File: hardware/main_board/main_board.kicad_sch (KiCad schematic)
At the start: 79 parts, among them J1 USB_C_Receptacle_USB2.0_16P, J2 UART_DEBUG, J3 BAT1, J4 Conn_02x05_Odd_Even, J5 Conn_02x05_Odd_Even, Q1 MMBT3904, Q2 MMBT3904, SW1 SW_MEC_5G, U1 MPU-6050, U10 AMS1117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

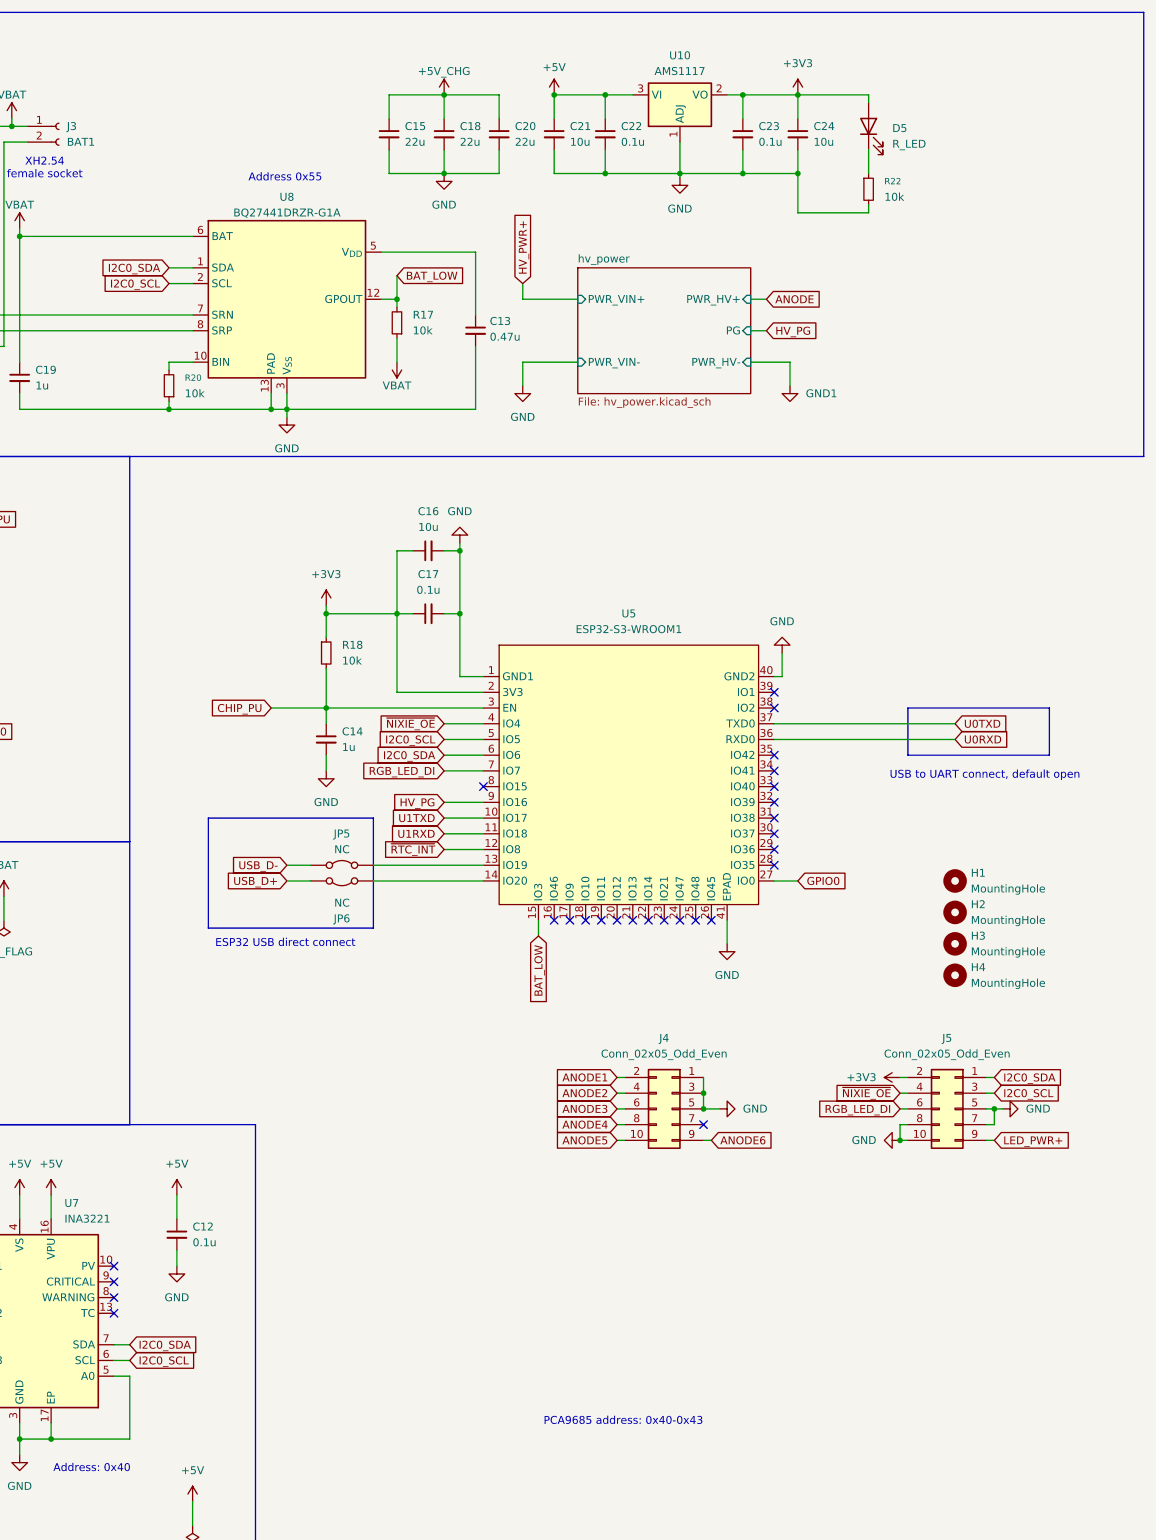
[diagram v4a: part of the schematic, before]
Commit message: WIP(haedware): add TPS62177 buck converter for 3v3 regulation
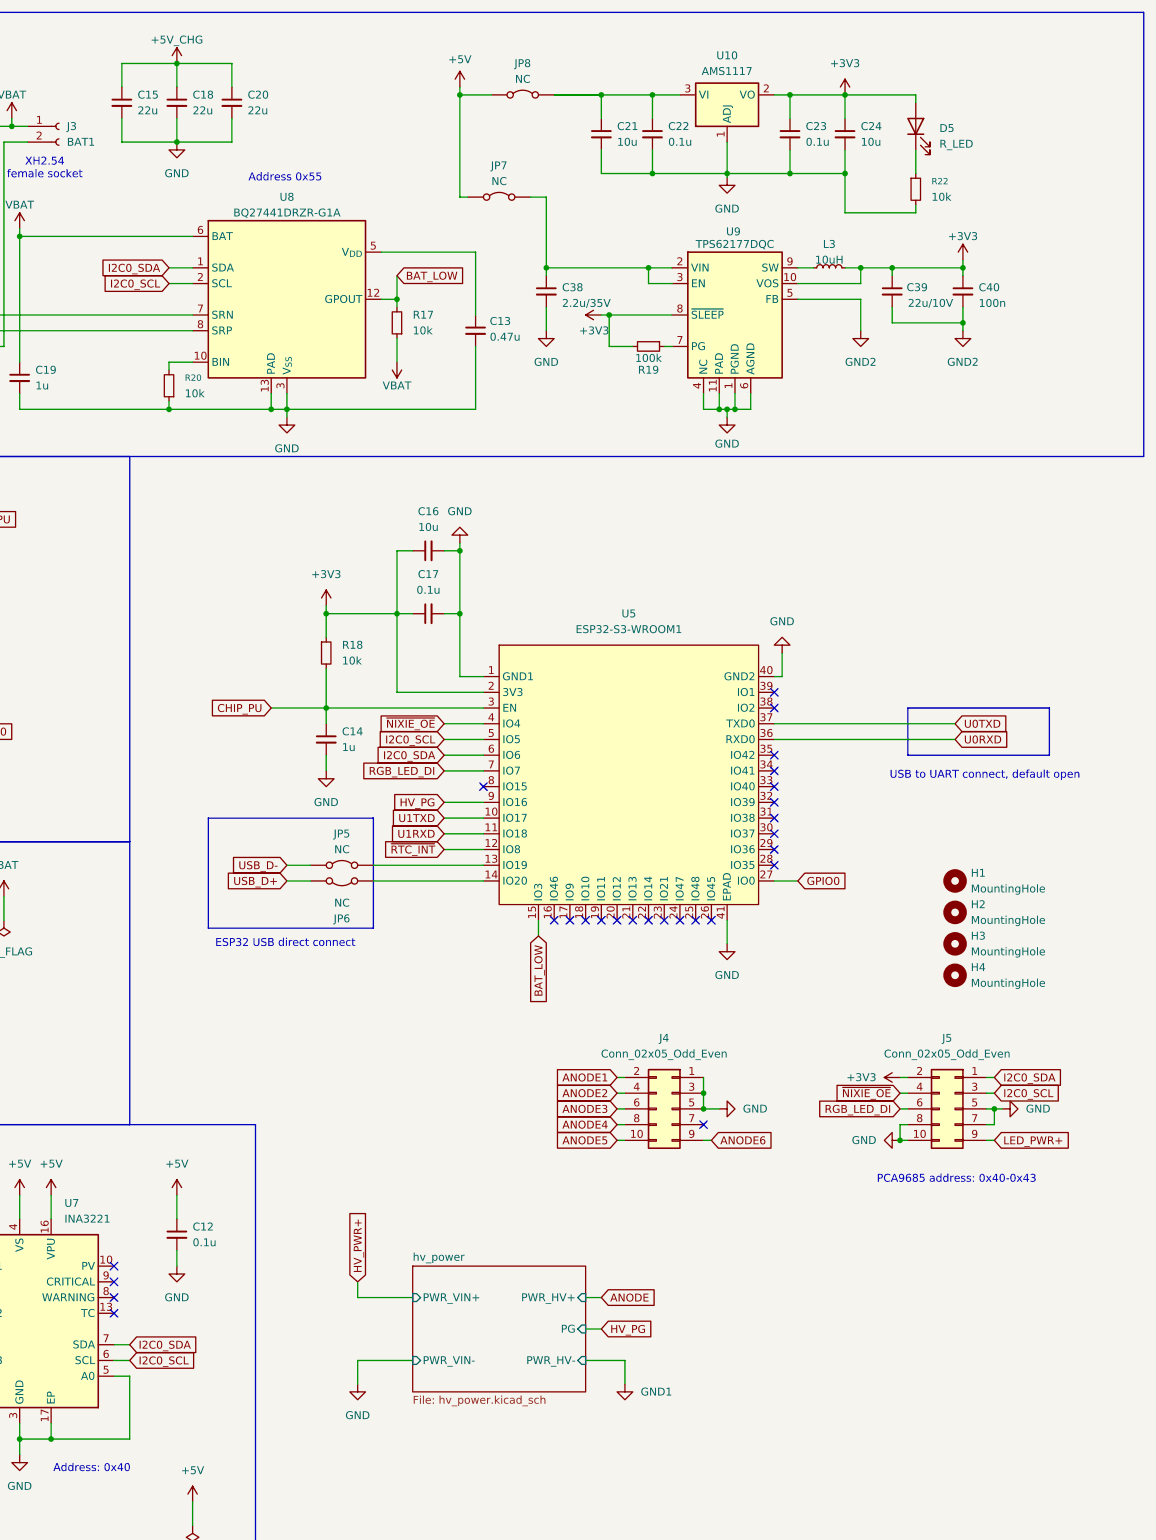
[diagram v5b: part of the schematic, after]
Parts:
- added C38: 2.2u/35V, Capacitor_SMD:C_0805_2012Metric, symbol Device:C_Small
- added C39: 22u/10V, Capacitor_SMD:C_1206_3216Metric, symbol Device:C_Small
- added C40: 100n, Capacitor_SMD:C_0402_1005Metric, symbol Device:C_Small
- added JP7, JP8: NC, Jumper:SolderJumper-2_P1.3mm_Bridged_RoundedPad1.0x1.5mm, symbol Jumper:Jumper_2_Bridged
- added L3: 10uH, Inductor_SMD:L_Changjiang_FNR4010S, symbol Device:L_Small
- added R19: 100k, Resistor_SMD:R_0402_1005Metric, symbol Device:R_Small
- added U9: TPS62177DQC, Package_SON:WSON-10-1EP_2x3mm_P0.5mm_EP0.84x2.4mm_ThermalVias, symbol Regulator_Switching:TPS62177DQC
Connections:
- net +3V3: now also C39.1, C40.1, L3.2, R19.2, U9.10 (VOS), U9.8 (~{SLEEP})
- net +5V: now also JP7.1 (A), JP8.1 (A); no longer C21.1, C22.1, U10.3 (VI)
- net GND: now also C38.2, U9.1 (PGND), U9.11 (PAD), U9.4 (NC), U9.6 (AGND)
- new net: C21.1, C22.1, JP8.2 (B), U10.3 (VI)
- new net: R19.1, U9.7 (PG)
- new net: C38.1, JP7.2 (B), U9.2 (VIN), U9.3 (EN)
- new net: L3.1, U9.9 (SW)
- new net GND2: C39.2, C40.2, U9.5 (FB)
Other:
- moved on the sheet: C15, C18, C20, C21, C22, C23, C24, D5, R22, U10

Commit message: WIP(hardware): update main board and mainboard layout
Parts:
- removed JP8: NC, Jumper:SolderJumper-2_P1.3mm_Bridged_RoundedPad1.0x1.5mm, symbol Jumper:Jumper_2_Bridged
- removed R3, R4: 10k, Resistor_SMD:R_0603_1608Metric, symbol Device:R_Small
- added C43: 0.1u, Capacitor_SMD:C_0603_1608Metric, symbol Device:C_Small
- added JP8: NO, Jumper:SolderJumper-2_P1.3mm_Open_RoundedPad1.0x1.5mm, symbol Jumper:Jumper_2_Open
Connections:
- net GND2 is gone; now on net GND: C39.2, C40.2, U9.5 (FB)
- net +3V3: now also C43.1
- net +5V: now also JP8.1 (A)
- net GND: now also C43.2
- net U1RXD: now also U5.35 (IO42); no longer U5.11 (IO18)
- net U1TXD: now also U5.34 (IO41); no longer U5.10 (IO17)
- net ~{RTC_INT}: now also U5.38 (IO2); no longer U5.12 (IO8)
- net at C21.1, C22.1, U10.3 (VI): now also JP8.2 (B)
- net nixie_anode_mux/T0: now reaches U5.17 (IO9)
- net nixie_anode_mux/T1: now reaches U5.18 (IO10)
- net nixie_anode_mux/T2: now reaches U5.19 (IO11)
- net ANODE1 renamed nixie_anode_mux/T0_E
- net ANODE2 renamed nixie_anode_mux/T1_E
- net ANODE3 renamed nixie_anode_mux/T2_E
- net ANODE4 renamed nixie_anode_mux/T3_E
- net ANODE5 renamed nixie_anode_mux/T4_E
- net ANODE6 renamed nixie_anode_mux/T5_E
- no-connect marks 66 -> 63
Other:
- added sheet nixie_anode_mux (nixie_anode_mux.kicad_sch)
- sheet hv_power ports: added GND; removed PWR_HV-, PWR_VIN-
- moved on the sheet: J4, J5

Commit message: chore(hardware): complete mainboard layout
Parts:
- removed JP1, JP2, JP3, JP4: NO, Jumper:SolderJumper-2_P1.3mm_Open_RoundedPad1.0x1.5mm, symbol Jumper:Jumper_2_Open
- removed JP5, JP6: NC, Jumper:SolderJumper-2_P1.3mm_Bridged_RoundedPad1.0x1.5mm, symbol Jumper:Jumper_2_Bridged
- removed SW1: SW_MEC_5G, Button_Switch_SMD:SW_Push_1P1T_XKB_TS-1187A, symbol Switch:SW_MEC_5G
- added JP1, JP2, JP3, JP4: NC, Jumper:SolderJumper-2_P1.3mm_Open_RoundedPad1.0x1.5mm, symbol Jumper:Jumper_2_Bridged
- added JP5, JP6: NO, Jumper:SolderJumper-2_P1.3mm_Open_RoundedPad1.0x1.5mm, symbol Jumper:Jumper_2_Open
- added SW1: SW_Push, Button_Switch_SMD:SW_SPST_CK_RS282G05A3, symbol Switch:SW_Push
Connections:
- net GND: now also SW1.2
- net U0RXD: now also JP3.2 (B)
- net U0TXD: now also JP4.2 (B)
- net USB_D+: now also JP2.1 (A), JP6.1 (A)
- net USB_D-: now also JP1.1 (A), JP5.1 (A)
- net at U5.13 (IO19): now also JP5.2 (B)
- net at U2.5 (D-): now also JP1.2 (B)
- net at J2.2 (Pin_2), U2.25 (RXD): now also JP4.1 (A)
- net at J2.3 (Pin_3), U2.26 (TXD): now also JP3.1 (A)
- net at U5.14 (IO20): now also JP6.2 (B)
- net at U2.4 (D+): now also JP2.2 (B)
- net at R9.1: now also SW1.1

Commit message: chore(hardware): update bom and LCSC SN
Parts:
- C38: LCSC PN (none) -> C19110
- C39: value 22u/10V -> 22u; LCSC PN (none) -> C86295
- C40: value 100n -> 0.1u; footprint Capacitor_SMD:C_0402_1005Metric -> Capacitor_SMD:C_0603_1608Metric; LCSC PN (none) -> C36911391
- J4, J5, JP1, JP2, JP3, JP4, LS1: now left out of the parts list
- L3: LCSC PN (none) -> C135244
- R19: LCSC PN (none) -> C60491
- U9: LCSC PN (none) -> C91241
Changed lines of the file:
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@@
 		(unit 1)
 		(exclude_from_sim no)
-		(in_bom yes)
+		(in_bom no)
 		(on_board yes)
 		(dnp no)
@@
 		(unit 1)
 		(exclude_from_sim no)
-		(in_bom yes)
+		(in_bom no)
 		(on_board yes)
 		(dnp no)
@@
 			)
 		)
-		(property "Value" "22u/10V"
+		(property "Value" "22u"
 			(at 365.76 65.405 0)
 			(effects
@@
 			)
 		)
+		(property "LCSC PN" "C86295"
+			(at 363.22 63.5 0)
+			(effects
+				(font
+					(size 1.27 1.27)
+				)
+				(hide yes)
+			)
+		)
 		(pin "1"
 		)
@@
 		(unit 1)
 		(exclude_from_sim no)
-		(in_bom yes)
+		(in_bom no)
 		(on_board yes)
 		(dnp no)
@@
 		(unit 1)
 		(exclude_from_sim no)
-		(in_bom yes)
+		(in_bom no)
 		(on_board yes)
 		(dnp no)
@@
 			)
 		)
+		(property "LCSC PN" "C60491"
+			(at 323.85 72.39 90)
+			(effects
+				(font
+					(size 1.27 1.27)
+				)
+				(hide yes)
+			)
+		)
 		(pin "1"
 		)
@@
 			)
 		)
+		(property "LCSC PN" "C19110"
+			(at 307.34 63.5 0)
+			(effects
+				(font
+					(size 1.27 1.27)
+				)
+				(hide yes)
+			)
+		)
 		(pin "1"
 		)
@@
 			)
 		)
+		(property "LCSC PN" "C91241"
+			(at 337.82 67.31 0)
+			(effects
+				(font
+					(size 1.27 1.27)
+				)
+				(hide yes)
+			)
+		)
 		(pin "1"
 		)
@@
 		(unit 1)
 		(exclude_from_sim no)
-		(in_bom yes)
+		(in_bom no)
 		(on_board yes)
 		(dnp no)
@@
 			)
 		)
-		(property "Value" "100n"
+		(property "Value" "0.1u"
 			(at 377.19 65.4113 0)
 			(effects
@@
 			)
 		)
-		(property "Footprint" "Capacitor_SMD:C_0402_1005Metric"
+		(property "Footprint" "Capacitor_SMD:C_0603_1608Metric"
 			(at 374.65 63.5 0)
 			(effects
@@
 			)
 		)
+		(property "LCSC PN" "C36911391"
+			(at 374.65 63.5 0)
+			(effects
+				(font
+					(size 1.27 1.27)
+				)
+				(hide yes)
+			)
+		)
 		(pin "1"
 		)
@@
 		(unit 1)
 		(exclude_from_sim no)
-		(in_bom yes)
+		(in_bom no)
 		(on_board yes)
 		(dnp no)
@@
 			)
 		)
+		(property "LCSC PN" "C135244"
+			(at 353.06 59.69 90)
+			(effects
+				(font
+					(size 1.27 1.27)
+				)
+				(hide yes)
+			)
+		)
 		(pin "1"
 		)
@@
 		(unit 1)
 		(exclude_from_sim no)
-		(in_bom yes)
+		(in_bom no)
 		(on_board yes)
 		(dnp no)
